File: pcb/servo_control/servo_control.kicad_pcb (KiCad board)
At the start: 2 copper layers, 94.6 x 66.7 mm, 62 parts, among them J1 Jack-DC, J10 Conn_01x03_Female, J11 Conn_01x03_Female, J12 Conn_01x03_Female, J13 Conn_01x03_Female, J14 Conn_01x03_Female, J15 Conn_01x03_Female, J16 Conn_01x03_Female, J17 Conn_01x03_Female, J18 Conn_01x03_Female, J19 Conn_01x03_Female, J2 YLIDAR X4, J20 Conn_01x03_Female, J21 Conn_01x06_Male, J22 GY-87, J3 Conn_01x03_Female, J4 Conn_01x03_Female, J5 Conn_01x03_Female, J6 Conn_01x03_Female, J7 Conn_01x03_Female, J8 Conn_01x03_Female, J9 Conn_01x03_Female, SW1 ESP_PROG, SW2 ESP_RST, U1 PCA9685PW, U2 LM317-3.3_SOT-223, U3 ESP32-WROOM-32, U4 MCP73213-A6SI/MF, U5 PCA9685PW, U6 LM317-5_SOT-223, U7 LT1085-ADJ

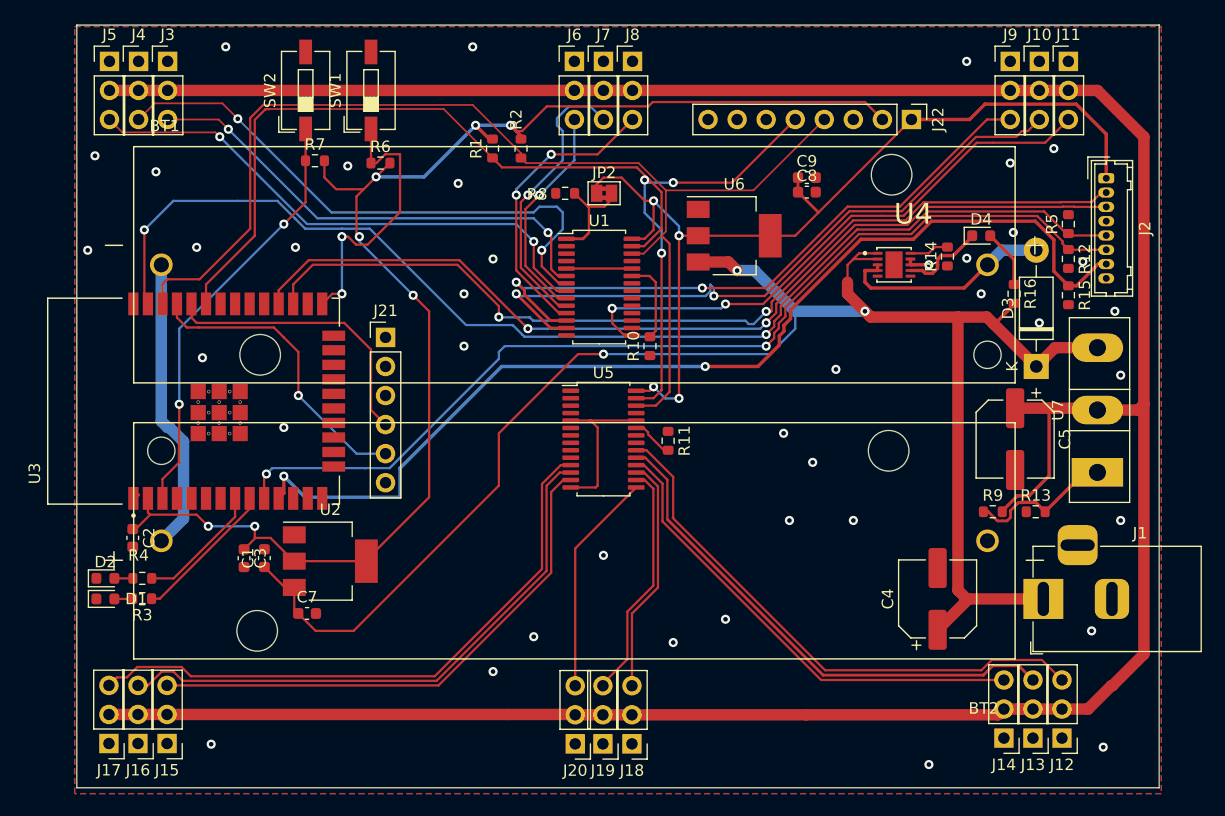
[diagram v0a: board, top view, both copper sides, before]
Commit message: add resistor current
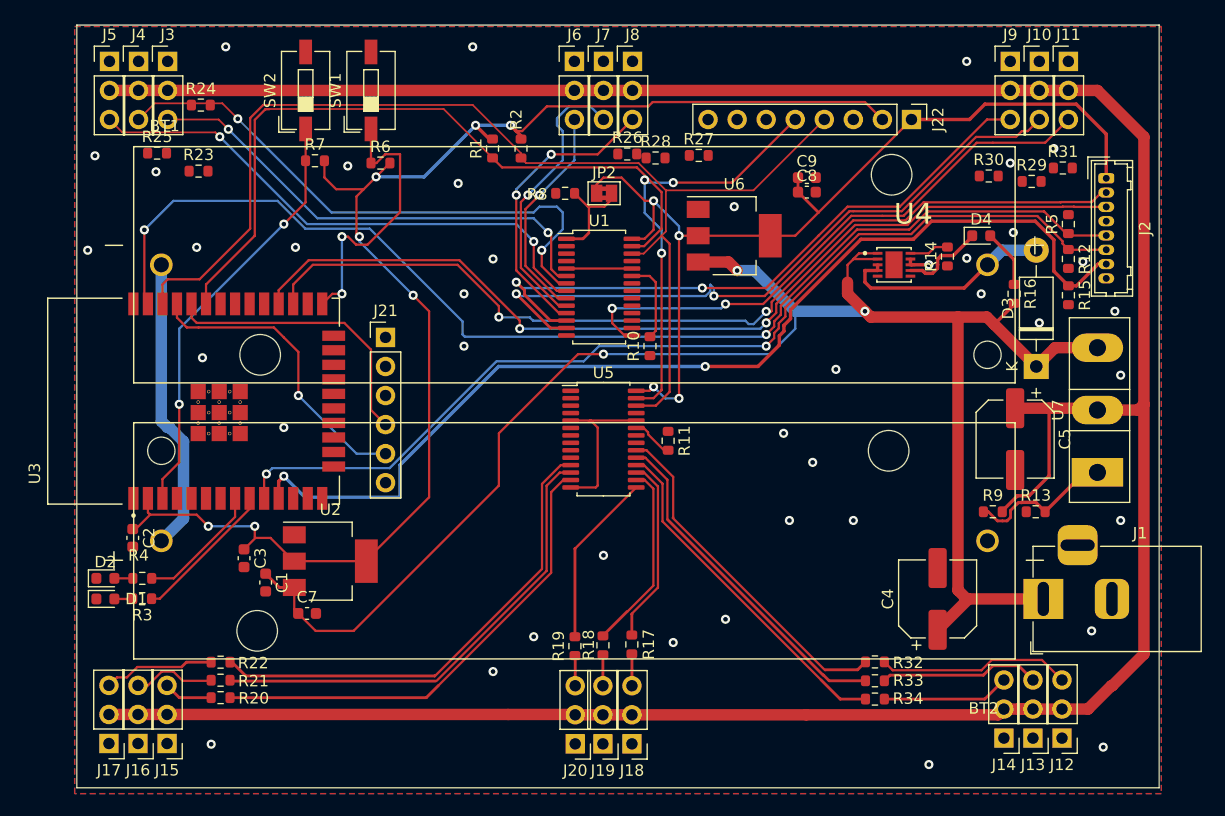
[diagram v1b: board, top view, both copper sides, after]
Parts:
- added R17: 10K, Resistor_SMD:R_0603_1608Metric, F.Cu at (149.8, 94.2)
- added R18: 10K, Resistor_SMD:R_0603_1608Metric, F.Cu at (147.3, 94.2)
- added R19: 10K, Resistor_SMD:R_0603_1608Metric, F.Cu at (144.8, 94.3)
- added R20: 10K, Resistor_SMD:R_0603_1608Metric, F.Cu at (113.8, 98.8)
- added R21: 10K, Resistor_SMD:R_0603_1608Metric, F.Cu at (113.8, 97.3)
- added R22: 10K, Resistor_SMD:R_0603_1608Metric, F.Cu at (113.8, 95.7)
- added R23: 10K, Resistor_SMD:R_0603_1608Metric, F.Cu at (111.9, 52.8)
- added R24: 10K, Resistor_SMD:R_0603_1608Metric, F.Cu at (112.1, 47.0)
- added R25: 10K, Resistor_SMD:R_0603_1608Metric, F.Cu at (108.3, 51.2)
- added R26: 10K, Resistor_SMD:R_0603_1608Metric, F.Cu at (149.4, 51.3)
- added R27: 10K, Resistor_SMD:R_0603_1608Metric, F.Cu at (155.7, 51.4)
- added R28: 10K, Resistor_SMD:R_0603_1608Metric, F.Cu at (151.9, 51.6)
- added R29: 10K, Resistor_SMD:R_0603_1608Metric, F.Cu at (184.8, 53.7)
- added R30: 10K, Resistor_SMD:R_0603_1608Metric, F.Cu at (181.0, 53.2)
- added R31: 10K, Resistor_SMD:R_0603_1608Metric, F.Cu at (187.5, 52.5)
- added R32: 10K, Resistor_SMD:R_0603_1608Metric, F.Cu at (171.1, 95.7)
- added R33: 10K, Resistor_SMD:R_0603_1608Metric, F.Cu at (171.1, 97.3)
- added R34: 10K, Resistor_SMD:R_0603_1608Metric, F.Cu at (171.1, 98.9)
- moved C1 2.14 mm to (117.8, 88.7), turned to -90 degrees
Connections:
- J10 pad 3: PWM_0_7 -> Net-(J10-Pad3)
- J11 pad 3: PWM_0_8 -> Net-(J11-Pad3)
- J12 pad 3: PWM_1_13 -> Net-(J12-Pad3)
- J13 pad 3: PWM_1_12 -> Net-(J13-Pad3)
- J14 pad 3: PWM_1_11 -> Net-(J14-Pad3)
- J15 pad 3: PWM_1_7 -> Net-(J15-Pad3)
- J16 pad 3: PWM_1_6 -> Net-(J16-Pad3)
- J17 pad 3: PWM_1_5 -> Net-(J17-Pad3)
- J18 pad 3: PWM_1_10 -> Net-(J18-Pad3)
- J19 pad 3: PWM_1_9 -> Net-(J19-Pad3)
- J20 pad 3: PWM_1_8 -> Net-(J20-Pad3)
- J3 pad 3: PWM_0_0 -> Net-(J3-Pad3)
- J4 pad 3: PWM_0_1 -> Net-(J4-Pad3)
- J5 pad 3: PWM_0_2 -> Net-(J5-Pad3)
- J6 pad 3: PWM_0_3 -> Net-(J6-Pad3)
- J7 pad 3: PWM_0_4 -> Net-(J7-Pad3)
- J8 pad 3: PWM_0_5 -> Net-(J8-Pad3)
- J9 pad 3: PWM_0_6 -> Net-(J9-Pad3)
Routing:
- net PWM_0_6: track 55.5 -> 0.00 mm, vias 2 -> 0
- net Net-(J9-Pad3): track 0.00 -> 55.5 mm, vias 0 -> 2
- net PWM_0_1: track 50.3 -> 0.00 mm, vias 2 -> 0
- net Net-(J4-Pad3): track 0.00 -> 50.3 mm, vias 0 -> 2
- net PWM_0_0: track 41.9 -> 0.00 mm, vias 2 -> 0
- net Net-(J3-Pad3): track 0.00 -> 41.9 mm, vias 0 -> 2
- net PWM_0_4: track 25.1 -> 0.00 mm, vias 1 -> 0
- net Net-(J7-Pad3): track 0.00 -> 25.1 mm, vias 0 -> 1
- net PWM_0_3: track 19.3 -> 0.00 mm, vias 1 -> 0
- net Net-(J6-Pad3): track 0.00 -> 19.3 mm, vias 0 -> 1
- net PWM_1_13: track 48.4 -> 30.4 mm
- net Net-(J12-Pad3): track 0.00 -> 16.9 mm
- net PWM_1_12: track 45.4 -> 30.1 mm
- net Net-(J13-Pad3): track 0.00 -> 14.0 mm
- net PWM_1_11: track 41.9 -> 30.4 mm
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
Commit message: move lidar wiring
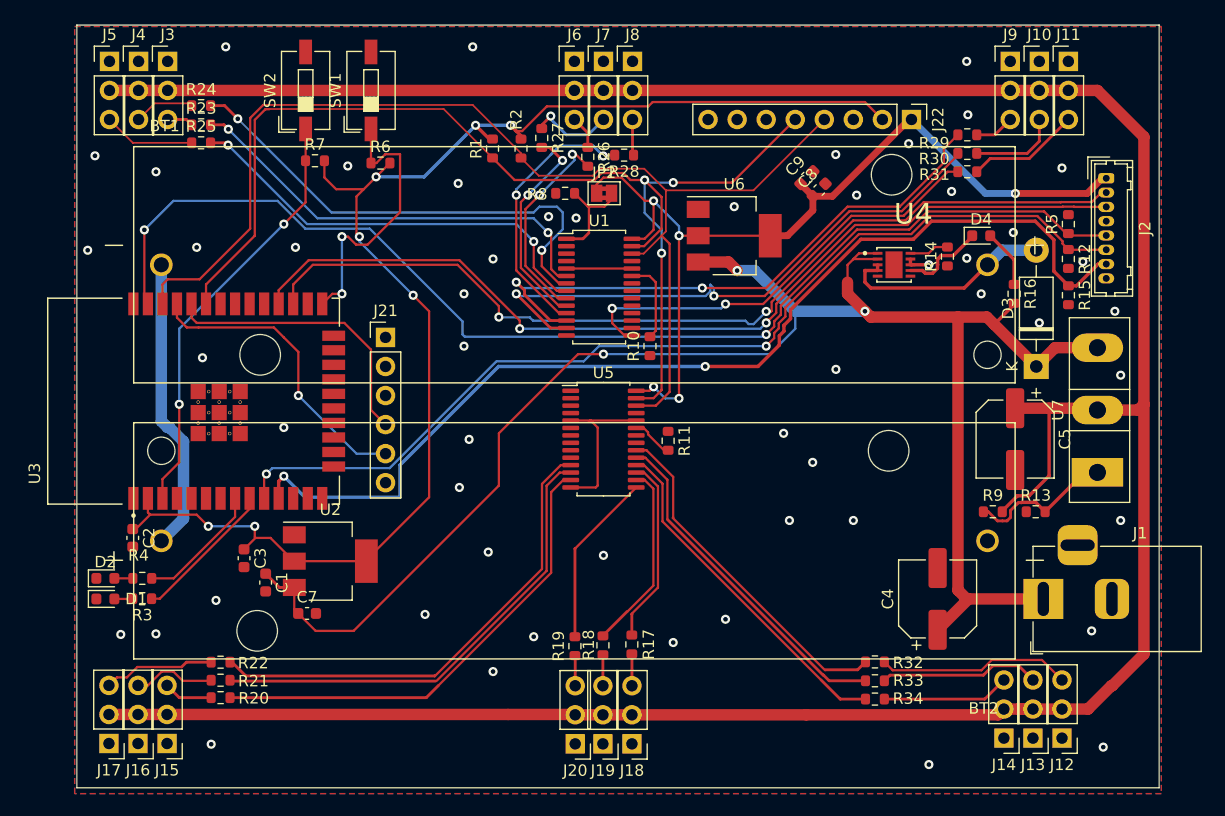
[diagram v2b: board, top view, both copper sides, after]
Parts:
- moved R27 13.8 mm to (141.9, 49.9), turned to -90 degrees
- moved R31 8.36 mm to (179.1, 52.8), turned to 180 degrees
- moved R29 6.95 mm to (179.1, 49.6), turned to 180 degrees
- moved R23 4.06 mm to (112.2, 48.7)
- moved R25 3.95 mm to (112.2, 50.3)
- moved R26 3.46 mm to (145.9, 51.5), turned to -90 degrees
- moved R28 2.76 mm to (149.1, 51.4), turned to 180 degrees
- moved R30 2.72 mm to (179.1, 51.2), turned to 180 degrees
- moved C8 1.09 mm to (166.2, 54.4), turned to 45 degrees
- moved R24 0.06 mm to (112.2, 47.0)
- turned C9 to 45 degrees
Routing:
- net Net-(J9-Pad3): track 55.5 -> 3.49 mm, vias 2 -> 0
- net PWM_0_6: track 0.00 -> 51.1 mm, vias 0 -> 2
- net Net-(J4-Pad3): track 50.3 -> 5.31 mm, vias 2 -> 0
- net PWM_0_1: track 0.00 -> 43.3 mm, vias 0 -> 2
- net Net-(J3-Pad3): track 41.9 -> 2.30 mm, vias 2 -> 0
- net PWM_0_0: track 0.00 -> 37.9 mm, vias 0 -> 2
- net PWM_0_4: track 0.00 -> 18.6 mm, vias 0 -> 2
- net PWM_0_3: track 0.00 -> 18.1 mm, vias 0 -> 2
- net Net-(J7-Pad3): track 25.1 -> 7.42 mm
- net Net-(J6-Pad3): track 19.3 -> 2.92 mm, vias 1 -> 0
- net PWM_0_8: track 50.2 -> 38.6 mm
- net Net-(J11-Pad3): track 0.00 -> 9.90 mm
- net PWM_0_2: track 47.5 -> 37.8 mm
- net PWM_0_7: track 59.4 -> 51.1 mm
- net Net-(J5-Pad3): track 0.00 -> 8.03 mm
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
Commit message: move pcf
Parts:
- moved C1 5.34 mm to (121.1, 93.0), turned to 0 degrees
- moved U5 4.98 mm to (147.2, 81.2)
- moved U1 2.81 mm to (146.9, 65.7)
- moved C9 2.21 mm to (165.1, 55.5), turned to 135 degrees
- moved C7 0.35 mm to (121.1, 91.3)
- moved C8 0.05 mm to (166.2, 54.5), turned to 135 degrees
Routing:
- net M_SCTR: track 103.4 -> 76.0 mm, vias 2 -> 1
- net PWM_1_13: track 30.4 -> 3.81 mm
- net PWM_1_12: track 30.1 -> 3.90 mm
- net PWM_1_11: track 30.4 -> 4.57 mm
- net ESP_TX: track 82.6 -> 60.8 mm, vias 2 -> 1
- net ESP_RX: track 81.4 -> 60.5 mm, vias 2 -> 1
- net 5V: track 80.8 -> 61.1 mm, vias 5 -> 3
- net 9V: track 152.7 -> 135.8 mm
- net PWM_1_9: track 16.5 -> 0.02 mm
- net PWM_1_10: track 16.3 -> 0.00 mm
- net I2C_SCL: track 102.5 -> 86.8 mm
- net PWM_1_8: track 15.3 -> 0.00 mm
- net DEV_EN: track 87.3 -> 72.7 mm, vias 2 -> 1
- net GND: track 22.4 -> 8.75 mm
- net I2C_SDA: track 101.2 -> 89.5 mm
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
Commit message: move pcf
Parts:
- removed BT1: 1043, 18650:BAT_1043
- moved R8 5.65 mm to (147.6, 59.0), turned to 90 degrees
- moved R11 5.25 mm to (152.9, 81.6)
- moved JP2 4.78 mm to (149.7, 58.9), turned to 90 degrees
- moved R10 1.76 mm to (152.3, 66.5)
- moved U5 1.38 mm to (146.8, 82.5)
- moved U1 0.53 mm to (146.9, 66.2)
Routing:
- net I2C_SDA: track 89.5 -> 54.1 mm, vias 3 -> 0
- net I2C_SCL: track 86.8 -> 56.1 mm
- net ESP_TX: track 60.8 -> 90.4 mm, vias 1 -> 2
- net ESP_RX: track 60.5 -> 87.6 mm, vias 1 -> 2
- net M_SCTR: track 76.0 -> 102.5 mm, vias 1 -> 2
- net PWM_1_13: track 3.81 -> 26.2 mm
- net PWM_1_12: track 3.90 -> 26.0 mm
- net PWM_1_11: track 4.57 -> 26.4 mm
- net 9V: track 135.8 -> 156.6 mm, vias 3 -> 2
- net 5V: track 61.1 -> 43.3 mm, vias 3 -> 1
- net DEV_EN: track 72.7 -> 86.9 mm, vias 1 -> 2
- net PWM_1_9: track 0.02 -> 10.2 mm
- net PWM_1_10: track 0.00 -> 9.74 mm
- net PWM_0_7: track 51.1 -> 42.1 mm
- net FIRST_A0: track 8.99 -> 0.00 mm
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
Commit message: rewire
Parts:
- added BT1: 1043, 18650:BAT_1043, F.Cu at (144.8, 61.0)
- moved J22 37.8 mm to (136.5, 47.9)
- moved R2 30.9 mm to (111.0, 61.0)
- moved R1 27.1 mm to (112.6, 61.0)
- moved BOOT 23.9 mm to (106.5, 58.0), turned to 180 degrees
- moved RST 16.6 mm to (106.5, 53.2), turned to 180 degrees
- moved R6 15.5 mm to (114.2, 59.4), turned to -90 degrees
- moved R7 9.84 mm to (115.8, 59.4), turned to -90 degrees
- renumbered SW1 to BOOT, SW2 to RST
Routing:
- net 5V: track 43.3 -> 98.6 mm, vias 1 -> 2
- net 3.3V: track 123.2 -> 94.4 mm, vias 7 -> 1
- net I2C_SDA: track 54.1 -> 76.8 mm, vias 0 -> 5
- net I2C_SCL: track 56.1 -> 78.1 mm, vias 0 -> 4
- net FIRST_A0: track 0.00 -> 7.97 mm
- net Net-(R6-Pad1): track 24.5 -> 19.0 mm
- net PWM_0_2: track 41.1 -> 45.5 mm, vias 2 -> 0
- net GND: track 2.38 -> 6.49 mm, vias 53 -> 61
- net PWM_0_6: track 43.1 -> 46.5 mm, vias 2 -> 0
- net PWM_0_7: track 42.1 -> 45.3 mm, vias 2 -> 0
- net FTDI_TX: track 25.1 -> 22.0 mm, vias 0 -> 1
- net PWM_0_0: track 42.2 -> 45.0 mm
- net ESP_RX: track 87.6 -> 89.5 mm
- net M_SCTR: track 102.5 -> 101.2 mm
- net Net-(R7-Pad1): track 37.5 -> 36.5 mm
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
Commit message: rewire
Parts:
- moved R27 5.67 mm to (147.2, 51.9)
- moved R9 2.97 mm to (184.3, 82.4)
- moved C2 2.72 mm to (103.9, 86.3), turned to 180 degrees
- moved R13 1.69 mm to (184.3, 84.0)
- moved C3 1.67 mm to (116.0, 88.3)
- moved R28 0.63 mm to (148.8, 51.9), turned to -90 degrees
- moved R26 0.48 mm to (145.7, 51.9)
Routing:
- net Net-(J7-Pad3): track 7.42 -> 2.85 mm, vias 1 -> 0
- net Net-(R13-Pad2): track 13.1 -> 10.9 mm
- net PWM_0_5: track 26.9 -> 24.9 mm
- net 6V: track 254.2 -> 252.3 mm
- net PWM_0_4: track 21.6 -> 23.4 mm
- net PWM_1_5: track 35.6 -> 34.0 mm
- net ESP_RX: track 89.5 -> 88.3 mm
- net PWM_0_2: track 45.5 -> 44.3 mm
- net 9V: track 156.6 -> 155.5 mm
- net Net-(R7-Pad1): track 36.5 -> 35.4 mm
- net 3.3V: track 94.4 -> 93.3 mm
- net ESP_TX: track 91.1 -> 90.3 mm
- net PWM_0_0: track 45.0 -> 44.1 mm
- net PWM_0_3: track 21.0 -> 21.8 mm
- net PWM_1_7: track 35.3 -> 34.6 mm
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
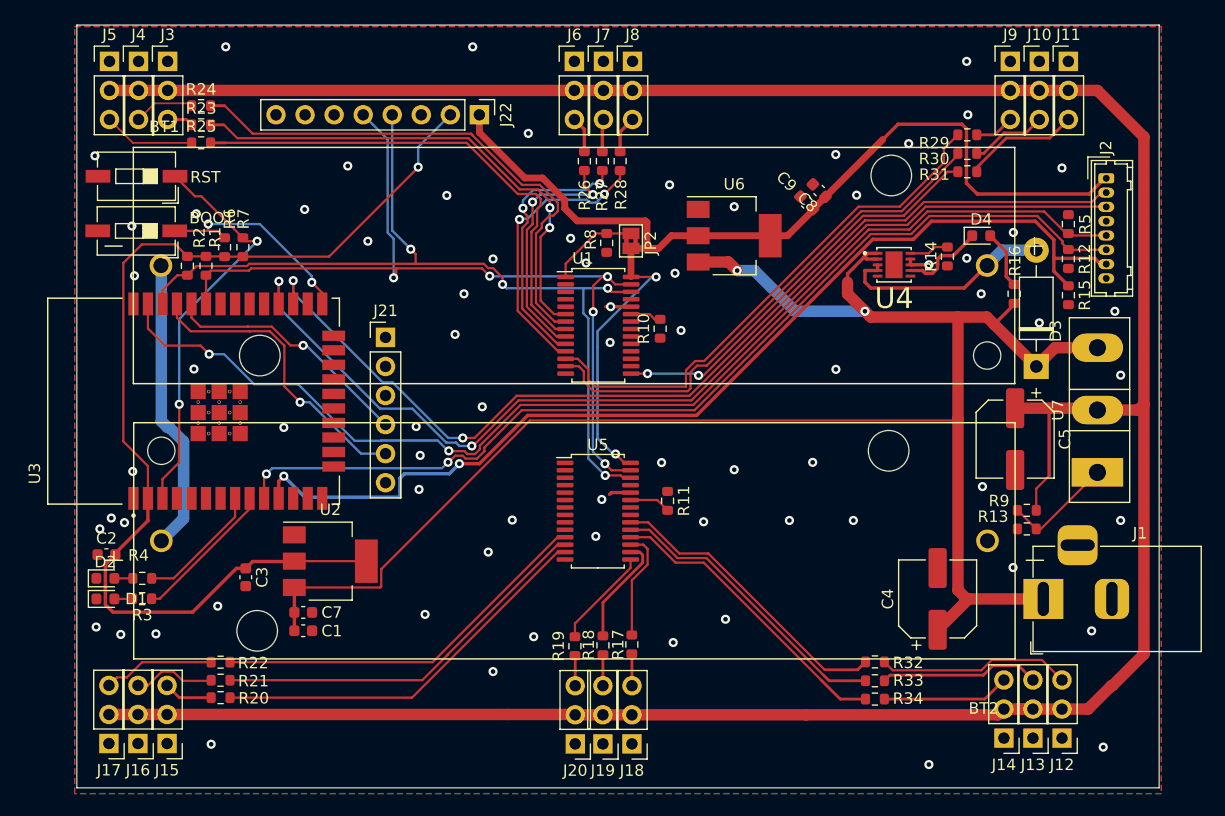
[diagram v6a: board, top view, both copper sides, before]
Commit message: add pcb atmega2560
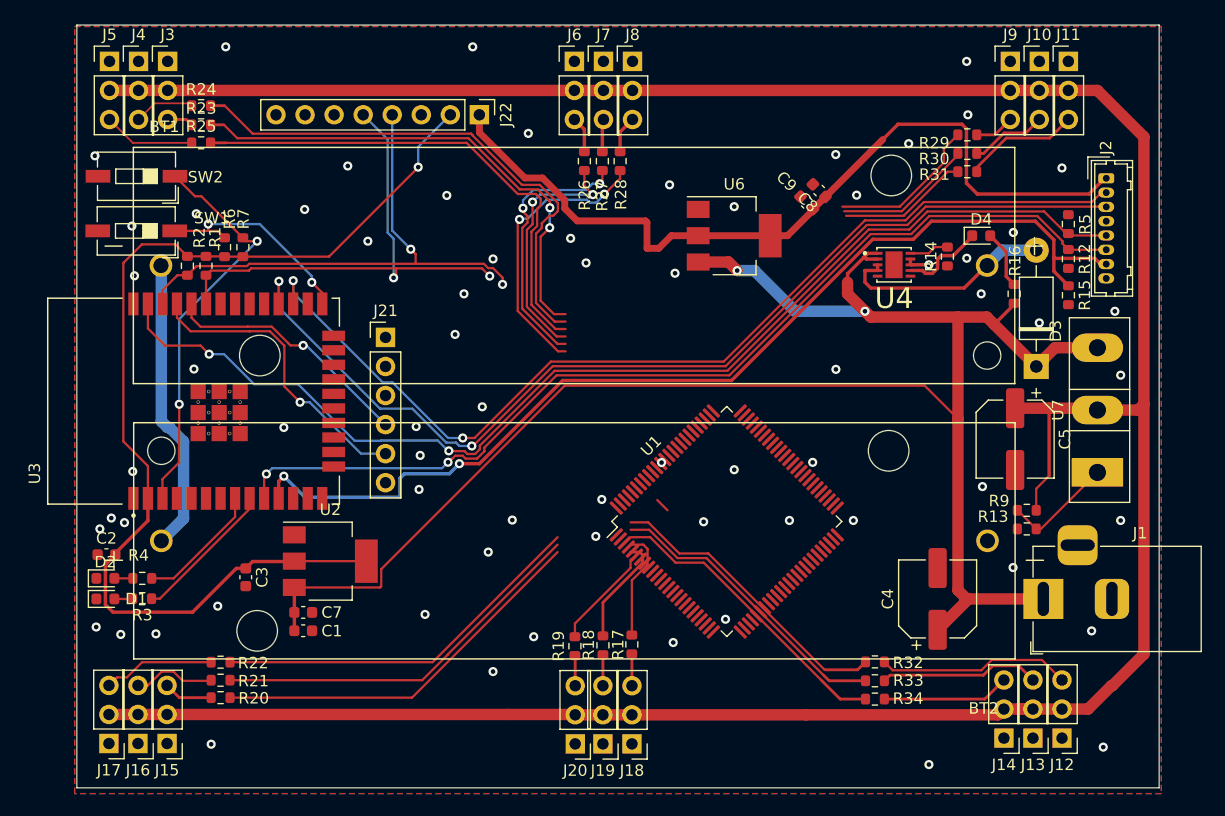
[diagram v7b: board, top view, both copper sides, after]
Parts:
- removed JP2: Jumper_2_Open, Jumper:SolderJumper-2_P1.3mm_Bridged2Bar_Pad1.0x1.5mm
- removed R10, R11, R8: 10K, Resistor_SMD:R_0603_1608Metric
- removed U5: PCA9685PW, Package_SO:TSSOP-28_4.4x9.7mm_P0.65mm
- U1: value PCA9685PW -> ATmega2560-16A; footprint Package_SO:TSSOP-28_4.4x9.7mm_P0.65mm -> Package_QFP:TQFP-100_14x14mm_P0.5mm
- moved U1 20.5 mm to (158.1, 83.4), turned to 45 degrees
- renumbered BOOT to SW1, RST to SW2
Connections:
- U1 pad 1: FIRST_A0 -> unconnected-(U1-PG5-Pad1)
- U1 pad 10: PWM_0_4 -> Net-(U1-VCC-Pad10)
- U1 pad 11: PWM_0_5 -> Net-(U1-GND-Pad11)
- U1 pad 12: PWM_0_6 -> unconnected-(U1-PH0-Pad12)
- U1 pad 13: PWM_0_7 -> unconnected-(U1-PH1-Pad13)
- U1 pad 14: GND -> unconnected-(U1-PH2-Pad14)
- U1 pad 15: PWM_0_8 -> unconnected-(U1-PH3-Pad15)
- U1 pad 16: PWM_0_9 -> unconnected-(U1-PH4-Pad16)
- U1 pad 17: PWM_0_10 -> unconnected-(U1-PH5-Pad17)
- U1 pad 18: PWM_0_11 -> unconnected-(U1-PH6-Pad18)
- U1 pad 19: PWM_0_12 -> unconnected-(U1-PB0-Pad19)
- U1 pad 2: GND -> unconnected-(U1-PE0-Pad2)
- U1 pad 20: PWM_0_13 -> unconnected-(U1-PB1-Pad20)
- U1 pad 21: PWM_0_14 -> unconnected-(U1-PB2-Pad21)
- U1 pad 22: PWM_0_15 -> unconnected-(U1-PB3-Pad22)
- U1 pad 23: Net-(R10-Pad2) -> unconnected-(U1-PB4-Pad23)
- U1 pad 24: GND -> unconnected-(U1-PB5-Pad24)
- U1 pad 25: GND -> unconnected-(U1-PB6-Pad25)
- U1 pad 26: I2C_SCL -> unconnected-(U1-PB7-Pad26)
- U1 pad 27: I2C_SDA -> unconnected-(U1-PH7-Pad27)
- U1 pad 28: 5V -> unconnected-(U1-PG3-Pad28)
- U1 pad 3: GND -> unconnected-(U1-PE1-Pad3)
- U1 pad 4: GND -> unconnected-(U1-PE2-Pad4)
- U1 pad 5: GND -> unconnected-(U1-PE3-Pad5)
- U1 pad 6: PWM_0_0 -> unconnected-(U1-PE4-Pad6)
- U1 pad 7: PWM_0_1 -> unconnected-(U1-PE5-Pad7)
- U1 pad 8: PWM_0_2 -> unconnected-(U1-PE6-Pad8)
- U1 pad 9: PWM_0_3 -> unconnected-(U1-PE7-Pad9)
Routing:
- net PWM_0_7: track 45.2 -> 12.1 mm
- net PWM_0_6: track 46.5 -> 13.4 mm
- net I2C_SDA: track 76.8 -> 44.1 mm, vias 5 -> 2
- net I2C_SCL: track 77.8 -> 46.8 mm, vias 4 -> 2
- net 5V: track 99.0 -> 72.7 mm, vias 2 -> 0
- net PWM_0_8: track 36.0 -> 11.4 mm, vias 2 -> 0
- net FIRST_A0: track 7.97 -> 0.00 mm
- net GND: track 6.49 -> 2.38 mm, vias 72 -> 69
- net Net-(R11-Pad2): track 3.61 -> 0.00 mm
- net Net-(R10-Pad2): track 2.72 -> 0.00 mm
- net 9V: track 155.5 -> 157.9 mm
- net (no net): track 0.00 -> 1.27 mm
- net PWM_1_7: track 34.6 -> 33.9 mm
- net PWM_1_6: track 34.2 -> 33.6 mm
- net PWM_1_5: track 34.0 -> 33.3 mm
